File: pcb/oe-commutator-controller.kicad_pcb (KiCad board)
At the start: 4 copper layers, 43 x 95 mm, 61 parts, among them J1 1719730004, U1 TEENSY-LC, U2 IS31FL3193, U3 TMC2130-LA, U4 PTN04050CAZ, U5 LTC4425

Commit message: Board revision C
- Sent to JLCPCB for testing
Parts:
- moved TP3 0.25 mm to (127.3, 109.6)
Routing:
- net GND: track 6.25 -> 31.3 mm
- net /OA1: track 28.1 -> 29.3 mm, vias 2 -> 3
- net /OB2: track 23.9 -> 25.1 mm, vias 2 -> 3
- net /OB1: track 27.0 -> 28.1 mm, vias 2 -> 3
- net /OA2: vias 2 -> 3

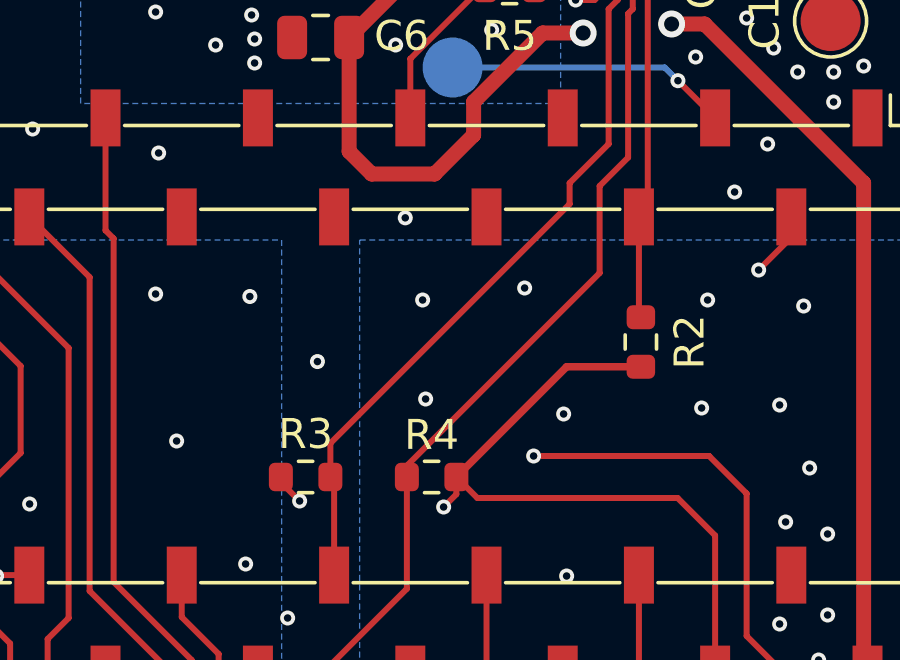
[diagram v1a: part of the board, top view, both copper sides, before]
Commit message: Increase R_prog to 2.49k
- This accounts for overhead current drawn from VCC by the Teensy and
  LED driver
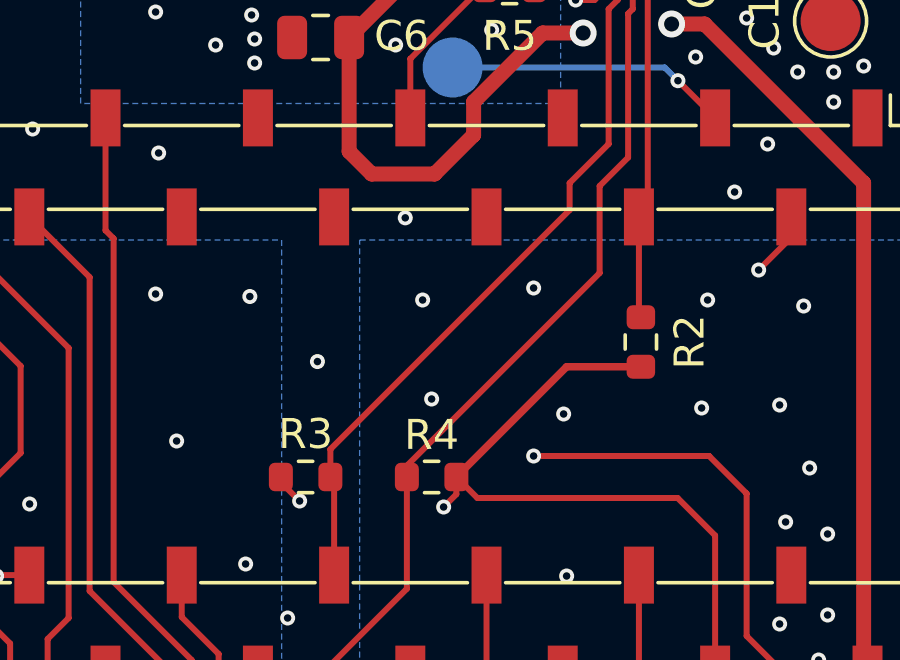
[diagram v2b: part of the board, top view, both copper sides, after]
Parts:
- C11, C17, C6: value 2.2uF -> 4.7uF
- R15: value 2k -> 2.49k
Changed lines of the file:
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@@
         (effects (font (size 1 1) (thickness 0.15)))
     )
-    (fp_text value "2.2uF" (at 0 1.68 90) (layer "F.Fab") hide
+    (fp_text value "4.7uF" (at 0 1.68 90) (layer "F.Fab") hide
         (effects (font (size 1 1) (thickness 0.15)))
     )
@@
         (effects (font (size 1 1) (thickness 0.15)))
     )
-    (fp_text value "2.2uF" (at 0 1.68) (layer "F.Fab") hide
+    (fp_text value "4.7uF" (at 0 1.68) (layer "F.Fab") hide
         (effects (font (size 1 1) (thickness 0.15)))
     )
@@
         (effects (font (size 1 1) (thickness 0.15)))
     )
-    (fp_text value "2k" (at 0 1.43) (layer "F.Fab") hide
+    (fp_text value "2.49k" (at 0 1.43) (layer "F.Fab") hide
         (effects (font (size 1 1) (thickness 0.15)))
     )
@@
         (effects (font (size 1 1) (thickness 0.15)))
     )
-    (fp_text value "2.2uF" (at 0 1.68 90) (layer "F.Fab") hide
+    (fp_text value "4.7uF" (at 0 1.68 90) (layer "F.Fab") hide
         (effects (font (size 1 1) (thickness 0.15)))
     )
@@
   (via (at 111.85 129.2) (size 0.5) (drill 0.25) (layers "F.Cu" "B.Cu") (net 2))
   (via (at 116.693763 58.550624) (size 0.5) (drill 0.25) (layers "F.Cu" "B.Cu") (net 2))
-  (via (at 130.3 72.4) (size 0.5) (drill 0.25) (layers "F.Cu" "B.Cu") (net 2))
+  (via (at 130.6 72.4) (size 0.5) (drill 0.25) (layers "F.Cu" "B.Cu") (net 2))
   (via (at 126.321294 70.06135) (size 0.5) (drill 0.25) (layers "F.Cu" "B.Cu") (net 2))
-  (via (at 127 76.1) (size 0.5) (drill 0.25) (layers "F.Cu" "B.Cu") (net 2))
+  (via (at 127.2 76.1) (size 0.5) (drill 0.25) (layers "F.Cu" "B.Cu") (net 2))
   (via (at 139.4 65.2) (size 0.5) (drill 0.25) (layers "F.Cu" "B.Cu") (net 2))
   (via (at 138.6 98.15) (size 0.5) (drill 0.25) (layers "F.Cu" "B.Cu") (net 2))
@@
   (segment (start 108.95 125.75) (end 111.1 125.75) (width 1) (layer "In1.Cu") (net 12))
   (segment (start 109.75 135) (end 108.45 133.7) (width 1) (layer "In1.Cu") (net 12))
-  (segment (start 131.8 69.6) (end 123.825 77.575) (width 0.2) (layer "F.Cu") (net 13))
-  (segment (start 133.1 67.6) (end 131.8 68.9) (width 0.2) (layer "F.Cu") (net 13))
+  (segment (start 123.825 77.775) (end 123.825 78.7) (width 0.2) (layer "F.Cu") (net 13))
   (segment (start 133.405 62.795) (end 133.1 63.1) (width 0.2) (layer "F.Cu") (net 13))
+  (segment (start 133.1 67.6) (end 131.8 68.9) (width 0.2) (layer "F.Cu") (net 13))
   (segment (start 123.95 78.825) (end 123.95 81.97) (width 0.2) (layer "F.Cu") (net 13))
-  (segment (start 123.825 77.575) (end 123.825 78.7) (width 0.2) (layer "F.Cu") (net 13))
+  (segment (start 131.8 68.9) (end 131.8 69.8) (width 0.2) (layer "F.Cu") (net 13))
+  (segment (start 131.8 69.8) (end 123.825 77.775) (width 0.2) (layer "F.Cu") (net 13))
+  (segment (start 133.405 61.86) (end 133.405 62.795) (width 0.2) (layer "F.Cu") (net 13))
   (segment (start 133.1 63.1) (end 133.1 67.6) (width 0.2) (layer "F.Cu") (net 13))
-  (segment (start 131.8 68.9) (end 131.8 69.6) (width 0.2) (layer "F.Cu") (net 13))
   (segment (start 123.95 78.825) (end 123.825 78.7) (width 0.2) (layer "F.Cu") (net 13))
-  (segment (start 133.405 61.86) (end 133.405 62.795) (width 0.2) (layer "F.Cu") (net 13))
   (segment (start 121.41 85.27) (end 123.53 85.27) (width 0.2) (layer "F.Cu") (net 14))
   (segment (start 126.375 78.7) (end 126.375 78.325) (width 0.2) (layer "F.Cu") (net 14))

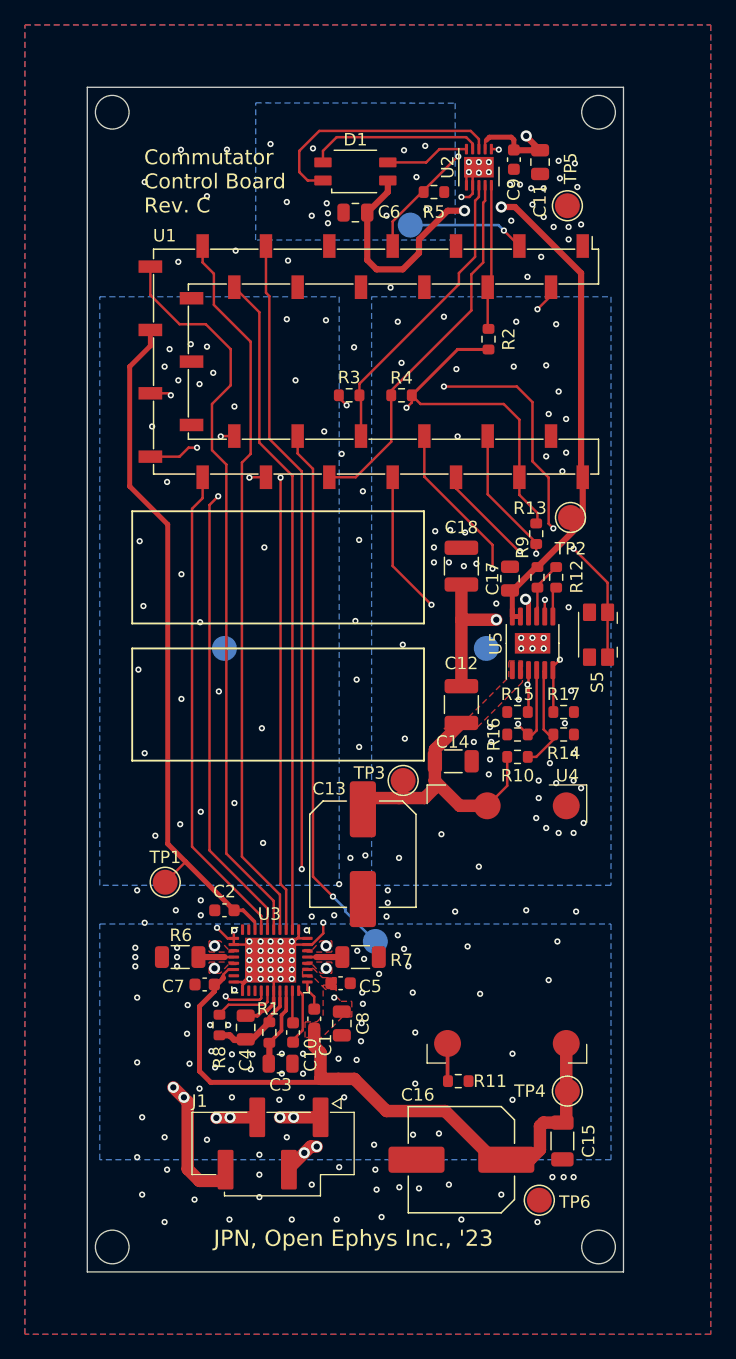
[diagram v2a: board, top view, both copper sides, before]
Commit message: Initial Rev D PCB component layout
- This is the initial component layout
- Some traces are routed, but a review seems wise before I grind
  out routing the rest of the traces and start resolving DRC
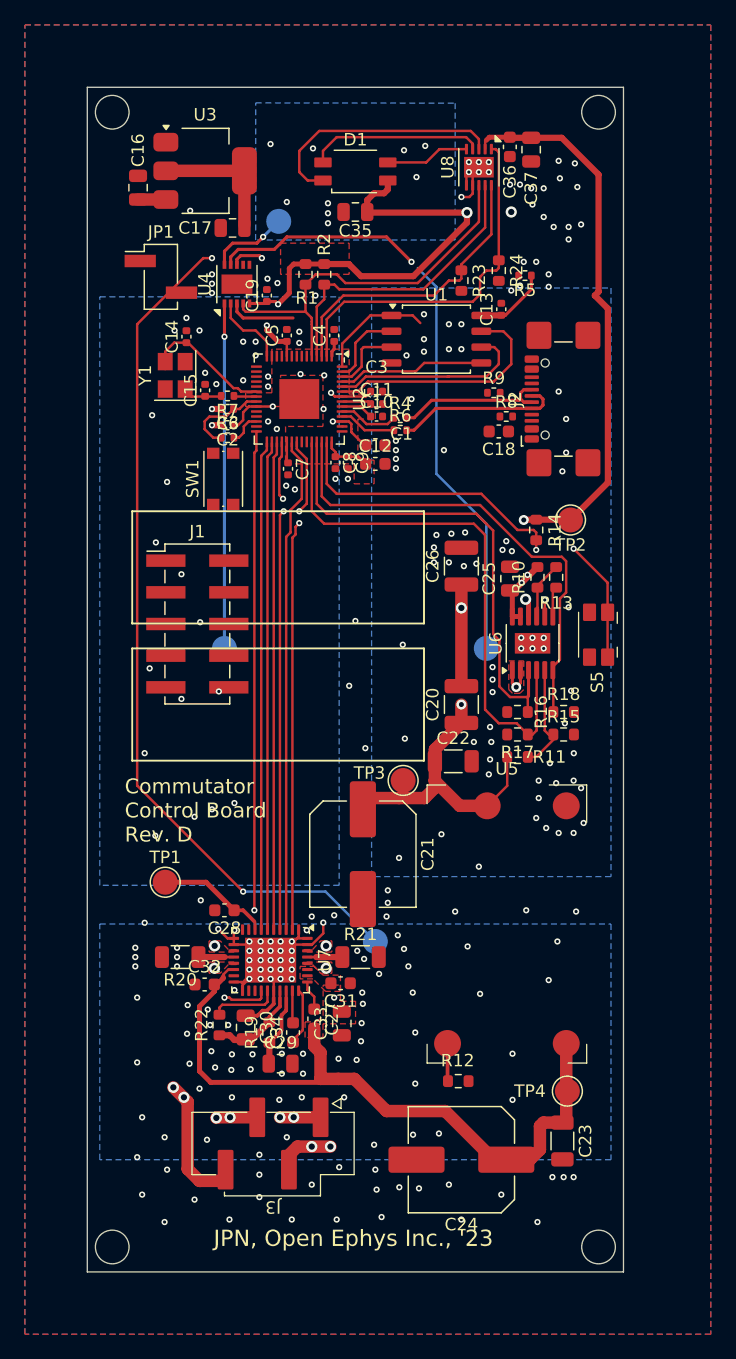
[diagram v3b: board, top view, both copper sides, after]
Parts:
- removed TP5, TP6: ~, TestPoint:TestPoint_Pad_D2.0mm
- added C19: 0.1uF, Capacitor_SMD:C_0402_1005Metric, F.Cu at (116.4, 70.7)
- added C20: HV0820-2R7305-R, Capacitor_SMD:C_1210_3225Metric, F.Cu at (132.0, 103.5)
- added C21: 100uF, Capacitor_SMD:C_Elec_8x10.2, F.Cu at (124.1, 115.5)
- added C22: 22uF, Capacitor_SMD:C_1206_3216Metric, F.Cu at (131.3, 108.0)
- added C23: 22uF, Capacitor_SMD:C_1206_3216Metric, F.Cu at (140.1, 138.5)
- added C24: 100uF, Capacitor_SMD:C_Elec_8x10.2, F.Cu at (132.0, 140.0)
- added C25: 4.7uF, Capacitor_SMD:C_0805_2012Metric, F.Cu at (135.9, 93.4)
- added C26: HV0820-2R7305-R, Capacitor_SMD:C_1210_3225Metric, F.Cu at (132.0, 92.4)
- added C27: 0.1uF, Capacitor_SMD:C_0603_1608Metric, F.Cu at (120.2, 128.7)
- added C28: 0.1uF, Capacitor_SMD:C_0603_1608Metric, F.Cu at (113.0, 120.0)
- added C29: 0.47uF, Capacitor_SMD:C_0805_2012Metric, F.Cu at (117.5, 132.3)
- added C30: 4.7uF, Capacitor_SMD:C_0805_2012Metric, F.Cu at (114.7, 129.4)
- added C31: 0.1uF, Capacitor_SMD:C_0603_1608Metric, F.Cu at (122.3, 125.8)
- added C32: 0.1uF, Capacitor_SMD:C_0603_1608Metric, F.Cu at (111.4, 126.0)
- added C33: 4.7uF, Capacitor_SMD:C_0805_2012Metric, F.Cu at (122.4, 129.1)
- added C34: 22nF, Capacitor_SMD:C_0603_1608Metric, F.Cu at (118.5, 129.8)
- added C35: 4.7uF, Capacitor_SMD:C_0805_2012Metric, F.Cu at (123.5, 64.0)
- added C36: 0.1uF, Capacitor_SMD:C_0603_1608Metric, F.Cu at (135.9, 58.8)
- added C37: 4.7uF, Capacitor_SMD:C_0805_2012Metric, F.Cu at (137.6, 59.0)
- added J2: USB4110-GF-A, Connector_USB:USB_C_Receptacle_GCT_USB4110, F.Cu at (141.3, 79.0)
- added J3: 1719730004, oe:MOLEX_1719730004_1x04_P2.54mm_Vert_Lock, F.Cu at (116.9, 138.7)
- added JP1: TSM-102-01-L-SV, Connector_PinHeader_2.54mm:PinHeader_1x02_P2.54mm_Vertical_SMD_Pin1Left, F.Cu at (107.9, 69.2)
- added R18: 10k, Resistor_SMD:R_0603_1608Metric, F.Cu at (140.2, 104.1)
- added R19: 2.2, Resistor_SMD:R_0603_1608Metric, F.Cu at (116.6, 129.8)
- added R20: 0.11,0.5W, Resistor_SMD:R_1206_3216Metric, F.Cu at (109.5, 123.8)
- added R21: 0.11,0.5W, Resistor_SMD:R_1206_3216Metric, F.Cu at (123.9, 123.8)
- added R22: 30k, Resistor_SMD:R_0603_1608Metric, F.Cu at (112.6, 129.2)
- added R23: 4.7k, Resistor_SMD:R_0603_1608Metric, F.Cu at (132.0, 69.5)
- added R24: 4.7k, Resistor_SMD:R_0603_1608Metric, F.Cu at (135.0, 68.7)
- added SW1: SW_Push, Button_Switch_SMD:SW_Push_1P1T_NO_CK_KMR2, F.Cu at (112.9, 85.4)
- added U6: LTC4425, Package_SO:MSOP-12-1EP_3x4mm_P0.65mm_EP1.65x2.85mm, F.Cu at (137.7, 98.6)
- added U7: TMC2130-LA, Package_DFN_QFN:QFN-36-1EP_5x6mm_P0.5mm_EP3.6x4.1mm, F.Cu at (116.7, 124.0)
- added U8: IS31FL3193, Package_DFN_QFN:DFN-10-1EP_3x3mm_P0.5mm_EP1.65x2.38mm, F.Cu at (133.4, 60.4)
- added Y1: ABM8AIG-12.000MHZ-12-2Z-T3, Crystal:Crystal_SMD_Abracon_ABM8AIG-4Pin_3.2x2.5mm, F.Cu at (109.0, 77.1)
- C1: value 0.1uF -> 1uF
- C10: value 22nF -> 0.1uF; footprint Capacitor_SMD:C_0603_1608Metric -> Capacitor_SMD:C_0402_1005Metric
- C11, C4, C6, C8: value 4.7uF -> 0.1uF; footprint Capacitor_SMD:C_0805_2012Metric -> Capacitor_SMD:C_0402_1005Metric
- C12: value HV0820-2R7305-R -> 1uF; footprint Capacitor_SMD:C_1210_3225Metric -> Capacitor_SMD:C_0603_1608Metric
- C13: value 100uF -> 0.1uF; footprint Capacitor_SMD:C_Elec_8x10.2 -> Capacitor_SMD:C_0402_1005Metric
- C14, C15: value 22uF -> 22pF; footprint Capacitor_SMD:C_1206_3216Metric -> Capacitor_SMD:C_0402_1005Metric
- C16: value 100uF -> 10u; footprint Capacitor_SMD:C_Elec_8x10.2 -> Capacitor_SMD:C_0805_2012Metric
- C17: value 4.7uF -> 10u
- C18: value HV0820-2R7305-R -> 0.1uF; footprint Capacitor_SMD:C_1210_3225Metric -> Capacitor_SMD:C_0603_1608Metric
- C2, C5, C7, C9: footprint Capacitor_SMD:C_0603_1608Metric -> Capacitor_SMD:C_0402_1005Metric
- C3: value 0.47uF -> 0.1uF; footprint Capacitor_SMD:C_0805_2012Metric -> Capacitor_SMD:C_0402_1005Metric
- J1: value 1719730004 -> 0015910100; footprint open-ephys:MOLEX_1719730004_1x04_P2.54mm_Vert_Lock -> Connector_PinHeader_2.54mm:PinHeader_2x05_P2.54mm_Vertical_SMD
- R1: value 2.2 -> 4.7k
- R10: value 160k -> 1.5M
- R11: value 1.33k -> 160k
- R12: value 1.2M -> 1.33k
- R13: value 10k -> 1.2M
- R14: value 51k -> 10k
- R15: value 2.49k -> 51k
- R16: value 10k -> 2.49k
- R3, R5: value 4.7k -> 10k; footprint Resistor_SMD:R_0603_1608Metric -> Resistor_SMD:R_0402_1005Metric
- R4: value 4.7k -> 27; footprint Resistor_SMD:R_0603_1608Metric -> Resistor_SMD:R_0402_1005Metric
- R6: value 0.11,0.5W -> 27; footprint Resistor_SMD:R_1206_3216Metric -> Resistor_SMD:R_0402_1005Metric
- R7: value 0.11,0.5W -> 1K; footprint Resistor_SMD:R_1206_3216Metric -> Resistor_SMD:R_0402_1005Metric
- R8: value 30k -> 5.1k; footprint Resistor_SMD:R_0603_1608Metric -> Resistor_SMD:R_0402_1005Metric
- R9: value 1.5M -> 5.1k; footprint Resistor_SMD:R_0603_1608Metric -> Resistor_SMD:R_0402_1005Metric
- S1, S2, S3, S4: footprint open-ephys:Touch_Center_2mm -> oe:Touch_Center_2mm
- U1: value TEENSY-LC -> W25Q128JVS; footprint open-ephys:PJRC_TEENSY_SMD -> Package_SO:SOIC-8_5.23x5.23mm_P1.27mm
- U2: value IS31FL3193 -> RP2040; footprint Package_DFN_QFN:DFN-10-1EP_3x3mm_P0.5mm_EP1.65x2.38mm -> Package_DFN_QFN:QFN-56-1EP_7x7mm_P0.4mm_EP3.2x3.2mm
- U3: value TMC2130-LA -> NCP1117-3.3_SOT223; footprint Package_DFN_QFN:QFN-36-1EP_5x6mm_P0.5mm_EP3.6x4.1mm -> Package_TO_SOT_SMD:SOT-223-3_TabPin2
- U4: value PTN04050CAZ -> CAP1296-x-AIA; footprint open-ephys:TI_R-PDSS_B4_SMD -> Package_DFN_QFN:DFN-10-1EP_3x3mm_P0.5mm_EP1.55x2.48mm
- U5: value LTC4425 -> PTN04050CAZ; footprint Package_SO:MSOP-12-1EP_3x4mm_P0.65mm_EP1.65x2.85mm -> oe:TI_R-PDSS_B4_SMD
- moved C16 82.1 mm to (106.1, 62.0), turned to 90 degrees
- moved C15 66.7 mm to (111.5, 78.3), turned to 90 degrees
- moved U3 63.5 mm to (111.5, 60.7), turned to 0 degrees
- moved R1 60.9 mm to (119.5, 69.0), turned to -90 degrees
- moved C4 56.0 mm to (121.8, 73.9), turned to 90 degrees
- moved U4 55.7 mm to (114.0, 69.8), turned to 90 degrees
- moved C3 54.4 mm to (125.2, 78.4)
- moved R8 53.9 mm to (135.6, 80.4), turned to 0 degrees
- moved C5 52.1 mm to (118.0, 73.9), turned to 90 degrees
- moved C10 49.9 mm to (125.2, 80.4), turned to 0 degrees
- moved C1 46.3 mm to (125.1, 82.7), turned to 0 degrees
- moved R7 46.2 mm to (113.2, 78.8), turned to 180 degrees
- moved R6 45.8 mm to (127.1, 81.5), turned to 0 degrees
- moved C13 45.1 mm to (135.2, 71.8), turned to 90 degrees
- moved C8 45.0 mm to (121.9, 84.1), turned to -90 degrees
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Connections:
- C1 pad 1: Net-(U3-VCP) -> Net-(U2-VREG_VOUT)
- C1 pad 2: +15V -> GND
- C10 pad 1: Net-(U3-CPO) -> +3.3V
- C10 pad 2: Net-(U3-CPI) -> GND
- C11 pad 1: VCC -> +3.3V
- C12 pad 1: +5V -> +3.3V
- C12 pad 2: Net-(U5-VMID) -> GND
- C13 pad 1: +5V -> +3.3V
- C14 pad 1: +5V -> Net-(U2-XIN)
- C15 pad 1: +15V -> Net-(C15-Pad1)
- C16 pad 1: +15V -> VBUS
- C17 pad 1: VCC -> +3.3V
- C18 pad 1: Net-(U5-VMID) -> VBUS
- C2 pad 1: +3.3V -> Net-(U2-VREG_VOUT)
- C3 pad 1: Net-(U3-VCC) -> Net-(U2-VREG_VOUT)
- C4 pad 1: GND -> +3.3V
- C4 pad 2: /TMC_{5V} -> GND
- C5 pad 1: GND -> +3.3V
- C5 pad 2: +15V -> GND
- C6 pad 1: VCC -> +3.3V
- C7 pad 1: GND -> +3.3V
- C7 pad 2: +15V -> GND
- C8 pad 1: GND -> +3.3V
- C8 pad 2: +15V -> GND
- C9 pad 1: VCC -> +3.3V
- D1 pad 2: VCC -> +3.3V
- J1 pad 1: /OA2 -> +3.3V
- J1 pad 2: /OA1 -> Net-(J1-Pin_2)
- J1 pad 3: /OB1 -> +3.3V
- J1 pad 4: /OB2 -> Net-(J1-Pin_4)
- R1 pad 1: Net-(U3-VCC) -> +3.3V
- R1 pad 2: /TMC_{5V} -> /MCU/SCL
- R10 pad 1: +5V -> +3.3V
- R10 pad 2: Net-(U5-FB) -> Net-(U6-PFI)
- R11 pad 1: Net-(U4-ADJ) -> +5V
- R11 pad 2: GND -> Net-(U6-FB)
- R12 pad 1: Net-(U5-PFI) -> Net-(U5-ADJ)
- R12 pad 2: Net-(U5-PFI_RET) -> GND
- R13 pad 1: /LTC44_{~{PFO}} -> Net-(U6-PFI)
- R13 pad 2: +3.3V -> Net-(U6-PFI_RET)
- R14 pad 1: Net-(U5-FB) -> /MCU/LTC44_{~{PFO}}
- R14 pad 2: GND -> +3.3V
- R15 pad 1: GND -> Net-(U6-FB)
- R15 pad 2: /LTC44_{CURR} -> GND
- R16 pad 1: /LTC44_{VMID} -> GND
- R16 pad 2: GND -> /MCU/LTC44_{CURR}
- R17 pad 1: /LTC44_{EN} -> /MCU/LTC44_{SEL}
- R2 pad 2: /IS31_{BM} -> /MCU/SDA
- R3 pad 2: /SCL -> /MCU/~{RESET}
- R4 pad 1: +3.3V -> Net-(U2-USB_DP)
- R4 pad 2: /SDA -> /MCU/D_{+}
- R5 pad 1: /IS31_{EN} -> +3.3V
- R5 pad 2: GND -> /MCU/QSPI_{~{CS}}
- R6 pad 1: Net-(U3-BRB) -> Net-(U2-USB_DM)
- R6 pad 2: GND -> /MCU/D_{-}
- R7 pad 1: Net-(U3-BRA) -> Net-(U2-XOUT)
- R7 pad 2: GND -> Net-(C15-Pad1)
- R8 pad 1: /TMC_{5V} -> GND
- R8 pad 2: Net-(U3-AIN_IREF) -> Net-(J2-CC1)
- R9 pad 1: VCC -> GND
- R9 pad 2: Net-(U5-PFI) -> Net-(J2-CC2)
- S1 pad 1: /CW -> /Touch Sensors/CCW
- S2 pad 1: /MODE -> /Touch Sensors/MODE
- S3 pad 1: /CCW -> /Touch Sensors/CW
- S4 pad 1: /STOP -> /Touch Sensors/STOP
- TP2 pad 1: VCC -> +5V
- TP3 pad 1: +5V -> +15V
- TP4 pad 1: +15V -> +3.3V
- U1 pad 1: GND -> /MCU/QSPI_{~{CS}}
- U1 pad 2: /CW -> /MCU/QSPI_{D1}
- U1 pad 3: /MODE -> /MCU/QSPI_{D2}
- U1 pad 4: /IS31_{BM} -> GND
- U1 pad 5: unconnected-(U1-3/PWM/T-Pad5) -> /MCU/QSPI_{D0}
- U1 pad 6: unconnected-(U1-4/PWM/T-Pad6) -> /MCU/QSPI_{CLK}
- U1 pad 7: /IS31_{EN} -> /MCU/QSPI_{D3}
- U1 pad 8: unconnected-(U1-6/CS1/PWM-Pad8) -> +3.3V
- U2 pad 1: /IS31_{EN} -> +3.3V
- U2 pad 10: /IS31_{BM} -> +3.3V
- U2 pad 11: GND -> unconnected-(U2-GPIO8-Pad11)
- U2 pad 2: VCC -> /MCU/IS31_{EN}
- U2 pad 3: Net-(D1-RK) -> /MCU/IS31_{BM}
- U2 pad 4: Net-(D1-GK) -> /MCU/SDA
- U2 pad 5: Net-(D1-BK) -> /MCU/SCL
- U2 pad 6: GND -> unconnected-(U2-GPIO4-Pad6)
- U2 pad 7: GND -> unconnected-(U2-GPIO5-Pad7)
- U2 pad 8: /SCL -> unconnected-(U2-GPIO6-Pad8)
- U2 pad 9: /SDA -> unconnected-(U2-GPIO7-Pad9)
- U3 pad 2: /TMC_{~{CS}} -> +3.3V
- U3 pad 3: /SCLK -> VBUS
- U4 pad 1: GND -> /Touch Sensors/CCW
- U4 pad 2: +5V -> /MCU/ALERT#
- U4 pad 3: Net-(U4-ADJ) -> /MCU/SCL
- U4 pad 4: +15V -> /MCU/SDA
- U5 pad 1: +5V -> GND
- U5 pad 3: /LTC44_{CURR} -> Net-(U5-ADJ)
- U5 pad 4: /LTC44_{VMID} -> +15V
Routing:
- net /Touch Sensors/STOP: track 0.00 -> 76.1 mm, vias 0 -> 3
- net VCC: track 74.9 -> 0.00 mm, vias 3 -> 0
- net /TMC_{EN}: track 69.9 -> 0.00 mm, vias 2 -> 0
- net /MISO: track 59.7 -> 0.00 mm
- net /MOSI: track 58.0 -> 0.00 mm
- net +3.3V: track 88.8 -> 145.2 mm, vias 2 -> 9
- net /TMC_{~{CS}}: track 53.5 -> 0.00 mm
- net /MCU/TMC_{EN}: track 0.00 -> 50.2 mm, vias 0 -> 2
- net /SCLK: track 48.2 -> 0.00 mm, vias 2 -> 0
- net Net-(S5-A): track 54.5 -> 9.83 mm, vias 4 -> 1
- net /MCU/LTC44_{SEL}: track 0.00 -> 44.1 mm
- net /STOP: track 43.1 -> 0.00 mm, vias 1 -> 0
- net /TMC_{STEP}: track 41.4 -> 0.00 mm, vias 2 -> 0
- net /MCU/TMC_{~{CS}}: track 0.00 -> 41.3 mm, vias 0 -> 2
- net /MCU/MOSI: track 0.00 -> 41.2 mm, vias 0 -> 2
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- added copper zone on B.Cu, net (none)
- added copper zone on F.Cu, net (none)
- added copper zone on F.Cu, net +3.3V
- added copper zone on B.Cu, net /MCU/IS31_{EN}
- added copper zone on B.Cu, net /MCU/SCL
- added copper zone on B.Cu, net /MCU/SDA
- removed copper zone on B.Cu, net /CCW
- removed copper zone on B.Cu, net /CW
- removed copper zone on B.Cu, net /MODE
- removed copper zone on F.Cu, net /OA1
- removed copper zone on F.Cu, net /OA2
- removed copper zone on F.Cu, net /OB1
- removed copper zone on F.Cu, net /OB2
- removed copper zone on B.Cu, net /STOP
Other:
- board text added: "Commutator Control Board Rev. D"
- board text removed: "Commutator Control Board Rev. C"

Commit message: Move stickers, silkscreen label, & header
- They were interfering in the previous commit
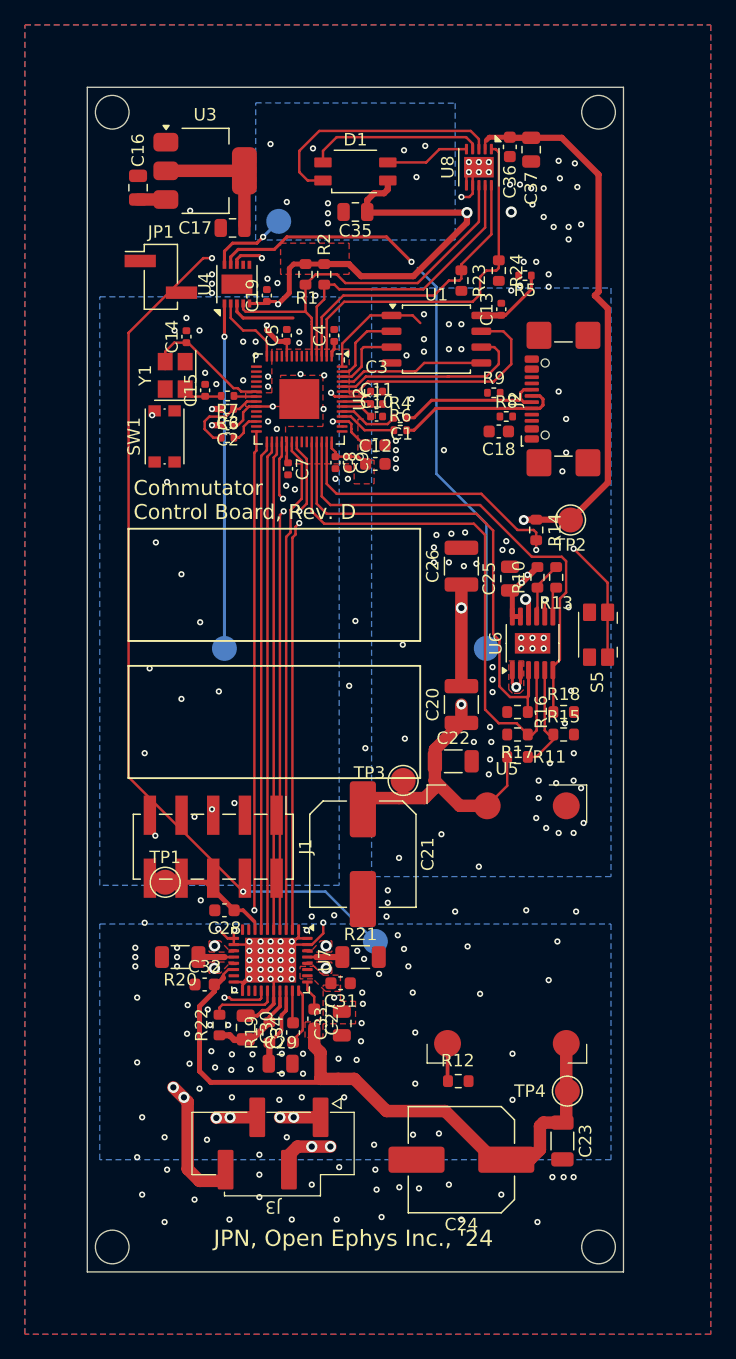
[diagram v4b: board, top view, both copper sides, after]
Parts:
- moved J1 17.9 mm to (112.1, 114.9), turned to -90 degrees
- moved SW1 5.80 mm to (108.2, 82.0)
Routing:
- net /Touch Sensors/STOP: track 76.1 -> 76.7 mm
- net GND: vias 256 -> 253
- net /MCU/~{RESET}: vias 0 -> 1
- net /MCU/GPIO_{1}: vias 1 -> 2
- net +3.3V: vias 9 -> 10
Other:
- board text added: "Commutator Control Board, Rev. D"
- board text added: "JPN, Open Ephys Inc., '24"
- board text removed: "Commutator Control Board Rev. D"
- board text removed: "JPN, Open Ephys Inc., '23"
